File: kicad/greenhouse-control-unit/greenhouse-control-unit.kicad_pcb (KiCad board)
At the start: 2 copper layers, 68 parts, among them J1 Pluggable_Terminal_01x02, J10 Conn_01x15_Female, J10_LittleBuck1 Conn_01x01_Female, J11 Molex_KK-254_01x03, J11_LittleBuck1 Conn_01x01_Female, J12 Molex_KK-396_01x16, J12_BigBuck1 Conn_01x01_Female, J13 Molex_KK-254_01x10, J13_BigBuck1 Conn_01x01_Female, J14 Molex_KK-254_01x02, J14_LittleBuck1 Conn_01x01_Female, J15_LittleBuck1 Conn_01x01_Female, J2 Pluggable_Terminal_01x02, J3 Pluggable_Terminal_01x02, J4 Molex_KK-254_01x02, J5 Molex_KK-254_01x03, J6 Molex_KK-254_01x02, J6_BigBuck1 Conn_01x01_Female, J7 Conn_01x10_Female, J7_BigBuck1 Conn_01x01_Female, J8 Conn_01x10_Female, J9 Conn_01x15_Female, Q1 2N7000, Q10 IRLB8721PBF, Q11 IRLB8721PBF, Q12 IRLB8721PBF, Q13 IRLB8721PBF, Q2 2N7000, Q3 2N7000, Q4 IRLB8721PBF, Q5 IRLB8721PBF, Q6 IRLB8721PBF, Q7 IRLB8721PBF, Q8 2N7000, Q9 2N7000, U1 74HC595, U2 74HC595

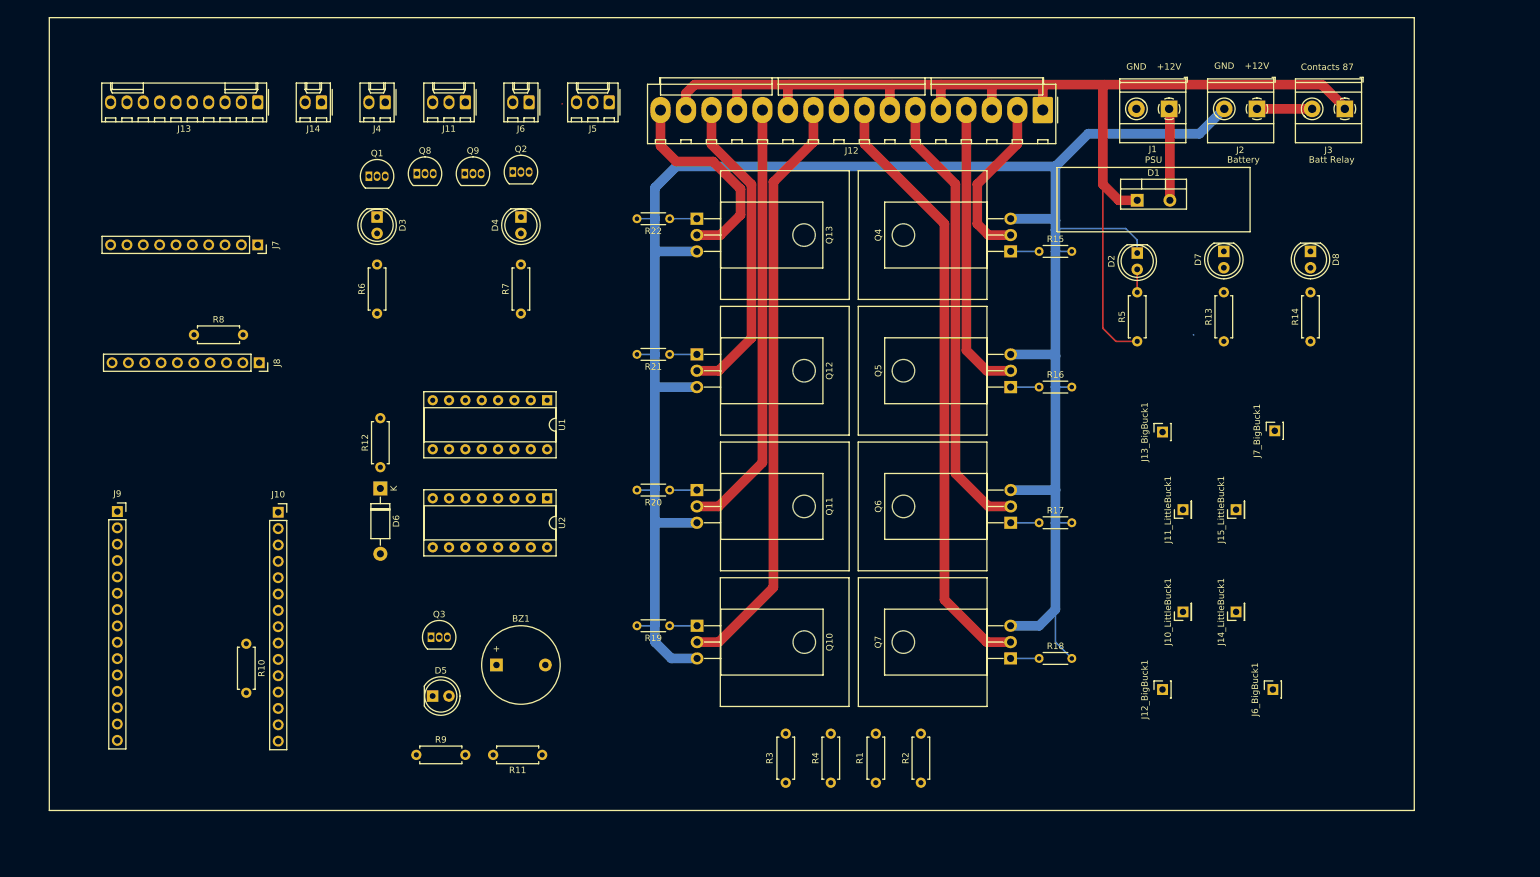
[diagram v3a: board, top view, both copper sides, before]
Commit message: Consolidate KK headers, connect all traces on PCB
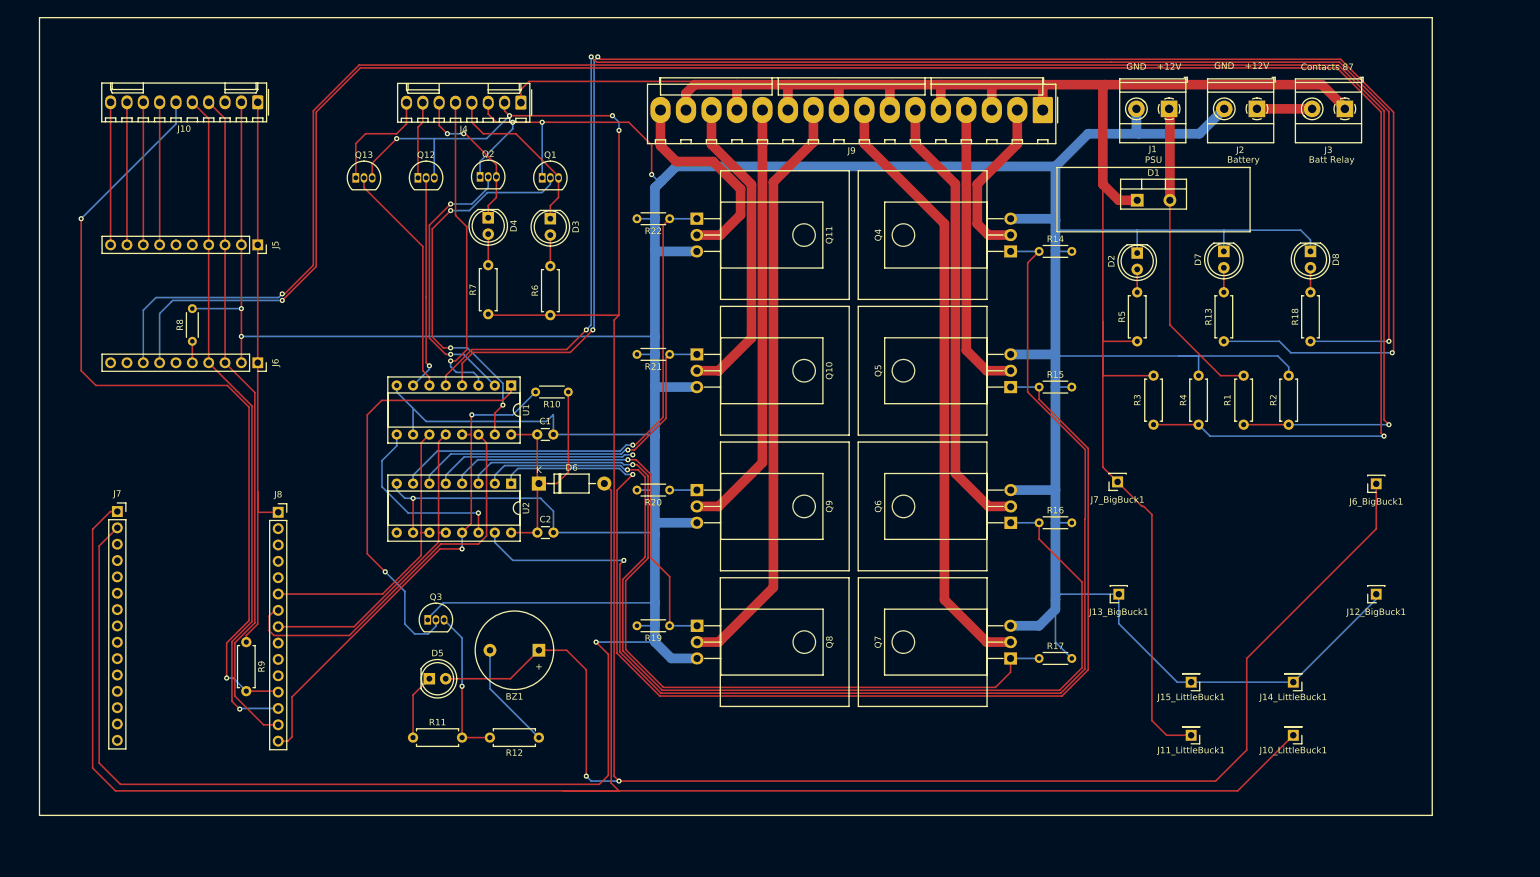
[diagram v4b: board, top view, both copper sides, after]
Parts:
- removed J11: Molex_KK-254_01x03, Connector_Molex:Molex_KK-254_AE-6410-03A_1x03_P2.54mm_Vertical
- removed J14: Molex_KK-254_01x02, Connector_Molex:Molex_KK-254_AE-6410-02A_1x02_P2.54mm_Vertical
- removed the J5 at (123.2, 39.1)
- removed the J6 at (110.7, 39.1)
- added C1: 0.01 μf, Capacitor_THT:C_Disc_D3.0mm_W1.6mm_P2.50mm, F.Cu at (112.0, 90.7)
- added C2: 0.01 μf, Capacitor_THT:C_Disc_D3.0mm_W1.6mm_P2.50mm, F.Cu at (112.0, 105.9)
- J4: value Molex_KK-254_01x02 -> Molex_KK-254_01x08; footprint Connector_Molex:Molex_KK-254_AE-6410-02A_1x02_P2.54mm_Vertical -> Connector_Molex:Molex_KK-254_AE-6410-08A_1x08_P2.54mm_Vertical
- R10: renamed from R12; footprint Resistor_THT:R_Axial_DIN0207_L6.3mm_D2.5mm_P7.62mm_Horizontal -> Resistor_THT:R_Axial_DIN0204_L3.6mm_D1.6mm_P5.08mm_Horizontal
- R8: footprint Resistor_THT:R_Axial_DIN0207_L6.3mm_D2.5mm_P7.62mm_Horizontal -> Resistor_THT:R_Axial_DIN0204_L3.6mm_D1.6mm_P5.08mm_Horizontal
- moved R2 79.8 mm to (228.8, 89.2)
- moved R4 79.8 mm to (214.8, 89.2)
- moved R1 79.8 mm to (221.8, 81.5)
- moved R3 79.8 mm to (207.8, 81.5)
- moved J12_BigBuck1 36.4 mm to (242.4, 115.5), turned to 180 degrees
- moved J6_BigBuck1 35.8 mm to (242.4, 98.3), turned to 180 degrees
- moved J11_LittleBuck1 35.1 mm to (213.6, 137.4), turned to 180 degrees
- moved R10 31.5 mm to (116.8, 84.1), turned to 180 degrees
- moved J15_LittleBuck1 27.7 mm to (213.6, 129.2), turned to 180 degrees
- moved D3 26.9 mm to (114.0, 57.1)
- moved R6 26.9 mm to (114.0, 72.1)
- moved Q1 26.9 mm to (112.8, 50.8)
- moved J13_BigBuck1 26.1 mm to (202.4, 115.5), turned to 180 degrees
- moved J10_LittleBuck1 25.7 mm to (229.5, 137.4), turned to 180 degrees
- moved J7_BigBuck1 25.7 mm to (202.2, 98.0), turned to 180 degrees
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- renumbered J13 to J10, J7 to J5, J8 to J6, J9 to J7, J10 to J8, J12 to J9, Q12 to Q10, Q13 to Q11, Q8 to Q12, Q9 to Q13, Q10 to Q8, Q11 to Q9, R9 to R11, R11 to R12, R15 to R14, R16 to R15, R17 to R16, R18 to R17, R14 to R18, R10 to R9
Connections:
- net /SR_Q6 renamed /Motor1_SR_Q6
- net /SR_Q7 renamed /Motor2_SR_Q7
- D4 pad 1: Net-(D4-Pad1) -> /CaseFan_FET
- J4 pad 2: /BattRelayNC_Coil -> +5V
- J5 pad 1: +5VA -> +3V3
- J6 pad 1: +5VA -> +3V3
- Q2 pad 3: Net-(D4-Pad1) -> /CaseFan_FET
- U1 pad 10: unconnected-(U1-Pad10) -> GND
- U2 pad 10: unconnected-(U2-Pad10) -> GND
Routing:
- net GND: track 332.7 -> 934.3 mm, vias 0 -> 7
- net +5V: track 0.03 -> 372.0 mm, vias 0 -> 6
- net /ADC2_A0: track 0.00 -> 317.2 mm, vias 0 -> 2
- net /ADC2_A1: track 0.00 -> 305.4 mm, vias 0 -> 2
- net +5VA: track 0.00 -> 291.0 mm
- net /BatteryLed_SR_Q4: track 0.00 -> 260.2 mm, vias 0 -> 3
- net /PsuLed_SR_Q5: track 0.00 -> 244.4 mm, vias 0 -> 3
- net /SW0_SR_Q08: track 4.42 -> 187.5 mm, vias 0 -> 1
- net /SW1_SR_Q09: track 4.42 -> 179.0 mm, vias 0 -> 1
- net /SW2_SR_Q10: track 4.41 -> 159.5 mm, vias 0 -> 1
- net /MC_D3: track 0.00 -> 128.7 mm, vias 0 -> 2
- net /SW3_SR_Q11: track 4.44 -> 127.5 mm, vias 0 -> 1
- net +12V: track 185.7 -> 299.8 mm
- net /ADC1_SCA: track 0.00 -> 105.9 mm, vias 0 -> 1
- net /ADC1_SCL: track 0.00 -> 105.1 mm
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
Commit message: Add mounting holes
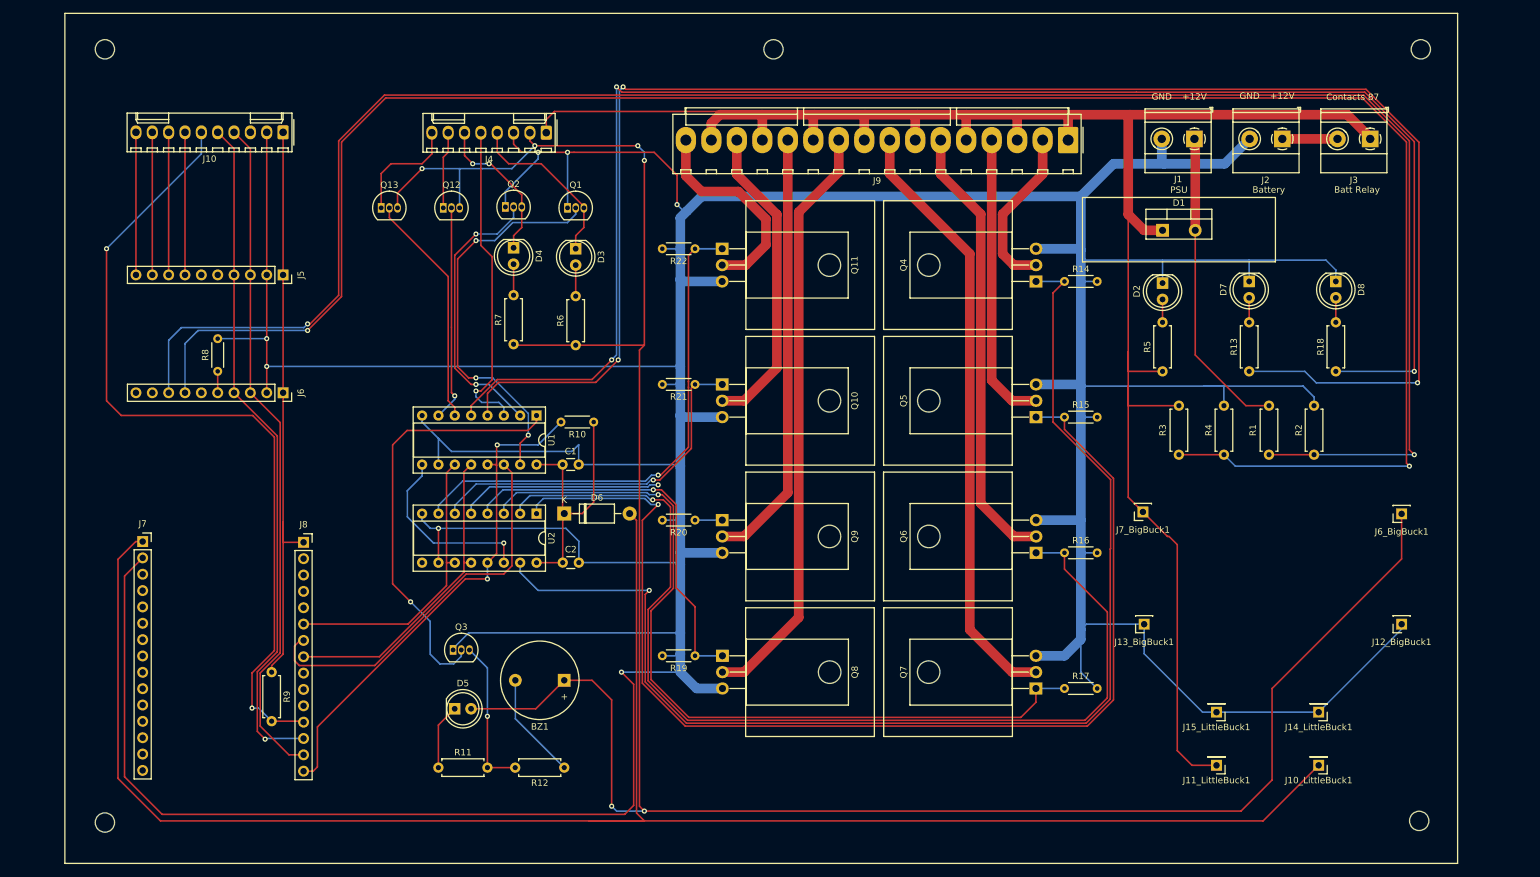
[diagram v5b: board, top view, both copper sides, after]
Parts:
- added H1: MountingHole, MountingHole:MountingHole_3mm, F.Cu at (44.8, 30.8)
- added H2: MountingHole, MountingHole:MountingHole_3mm, F.Cu at (249.3, 30.8)
- added H3: MountingHole, MountingHole:MountingHole_3mm, F.Cu at (44.8, 151.0)
- added H4: MountingHole, MountingHole:MountingHole_3mm, F.Cu at (249.0, 150.7)
- added H6: MountingHole, MountingHole:MountingHole_3mm, F.Cu at (148.7, 30.8)
- moved J6_BigBuck1 6.11 mm to (246.3, 103.0)
- moved Q9 6.11 mm to (140.8, 104.0)
- moved R20 6.11 mm to (136.5, 104.0)
- moved D7 6.11 mm to (222.6, 66.9)
- moved Q4 6.11 mm to (189.5, 66.9)
- moved R14 6.11 mm to (193.9, 66.9)
- moved R22 6.11 mm to (136.5, 61.8)
- moved J10_LittleBuck1 6.11 mm to (233.4, 142.1)
- moved J11_LittleBuck1 6.11 mm to (217.6, 142.1)
- moved BZ1 6.11 mm to (116.2, 128.9)
- moved J1 6.11 mm to (214.1, 44.7)
- moved J12_BigBuck1 6.11 mm to (246.3, 120.2)
- moved J13_BigBuck1 6.11 mm to (206.3, 120.2)
- moved J7_BigBuck1 6.11 mm to (206.1, 102.7)
- moved Q5 6.11 mm to (189.5, 88.0)
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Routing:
- net +5VA: track 291.0 -> 289.2 mm
- net GND: track 934.3 -> 932.8 mm
